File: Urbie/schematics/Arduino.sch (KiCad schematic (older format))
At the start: 1 part

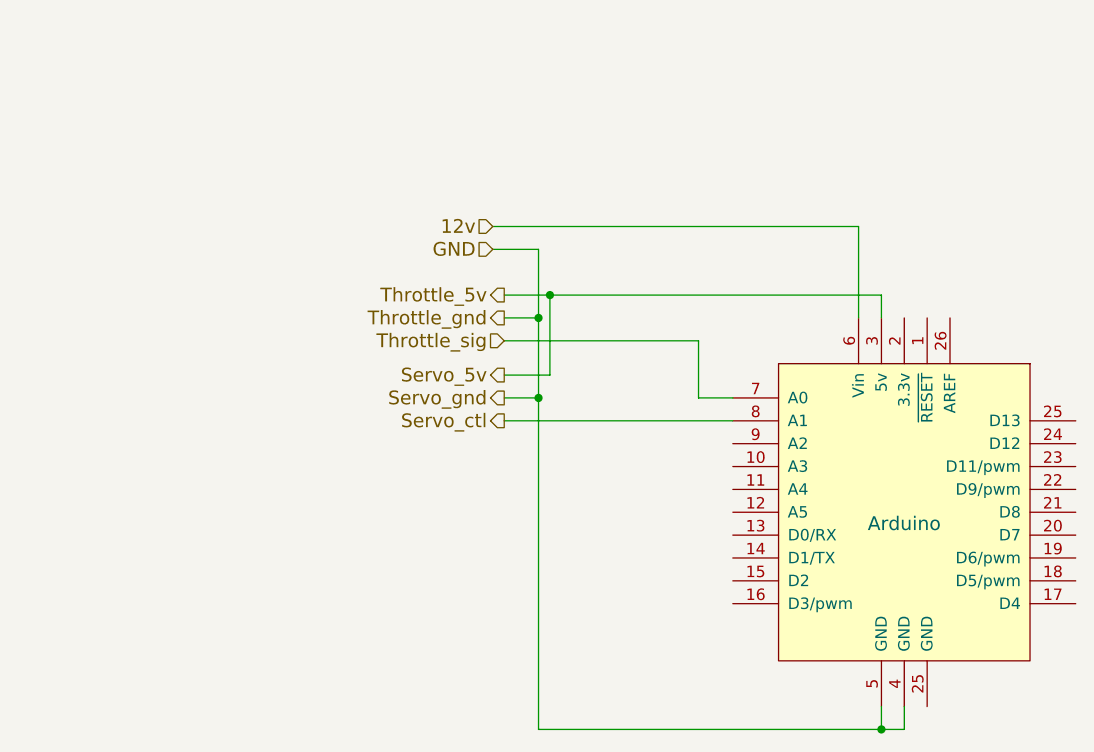
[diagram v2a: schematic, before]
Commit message: added DPDT switch for Hazard lights on Urbie
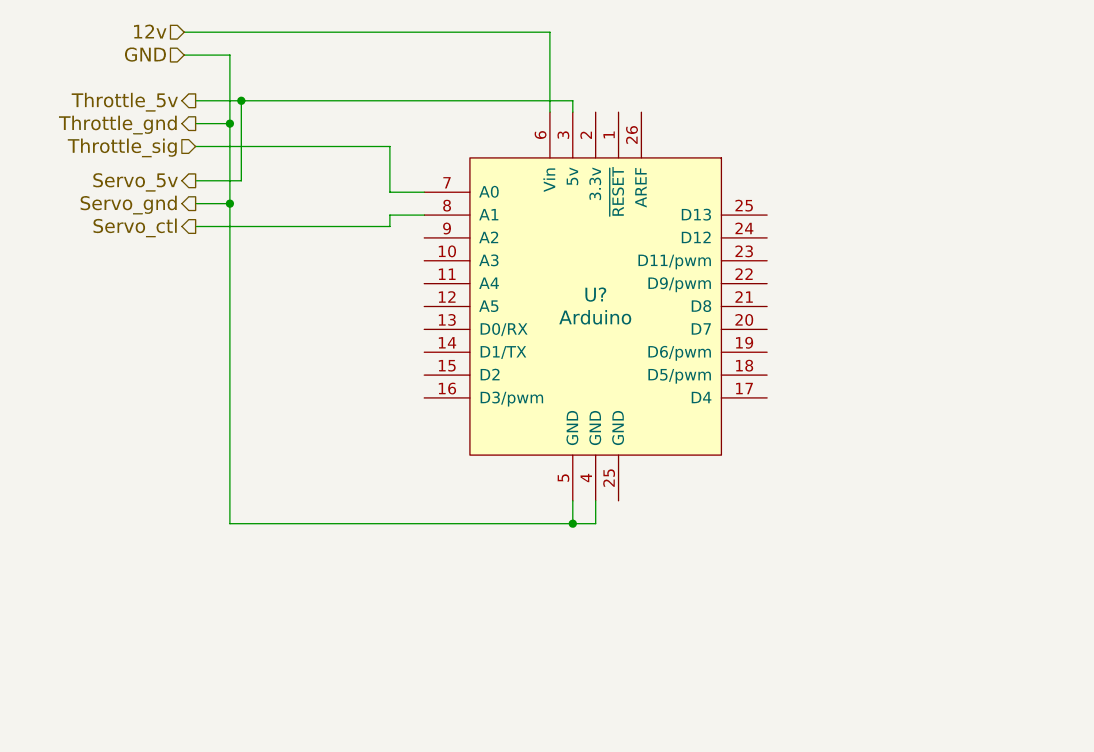
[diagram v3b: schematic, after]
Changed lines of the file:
@@
 LIBS:Supermileage
 LIBS:UrbieSchematics-cache
-LIBS:EFI_Breakout-cache
 EELAYER 25 0
 EELAYER END
 $Descr USLetter 11000 8500
 encoding utf-8
-Sheet 4 6
-Title "Urbie - Gasoline Urban Concept"
-Date "2016-11-19"
+Sheet 5 6
+Title "Sting - Gasoline Prototype"
+Date ""
 Rev ""
 Comp "Cedarville University"
-Comment1 "Tineka Witt"
+Comment1 "Samuel Ellicott"
 Comment2 "Arduino wiring connections"
 Comment3 ""
@@
 L Arduino U?
 U 1 1 57A2439F
-P 5900 4200
-F 0 "U?" H 5900 4250 60  0001 C CNN
-F 1 "Arduino" H 5900 4150 60  0000 C CNN
-F 2 "" H 5900 4500 60  0000 C CNN
-F 3 "" H 5900 4500 60  0000 C CNN
-	1    5900 4200
+P 4550 3300
+F 0 "U?" H 4550 3350 60  0000 C CNN
+F 1 "Arduino" H 4550 3250 60  0000 C CNN
+F 2 "" H 4550 3600 60  0000 C CNN
+F 3 "" H 4550 3600 60  0000 C CNN
+	1    4550 3300
 	1    0    0    -1
 $EndComp
-Text HLabel 4100 2950 0    60   Input ~ 0
+Text HLabel 2750 2100 0    60   Input ~ 0
 12v
-Text HLabel 4100 3050 0    60   Input ~ 0
+Text HLabel 2750 2200 0    60   Input ~ 0
 GND
-Text HLabel 4150 3250 0    60   Output ~ 0
+Text HLabel 2800 2400 0    60   Output ~ 0
 Throttle_5v
-Text HLabel 4150 3350 0    60   Output ~ 0
+Text HLabel 2800 2500 0    60   Output ~ 0
 Throttle_gnd
-Text HLabel 4150 3450 0    60   Input ~ 0
+Text HLabel 2800 2600 0    60   Input ~ 0
 Throttle_sig
-Text HLabel 4150 3600 0    60   Output ~ 0
+Text HLabel 2800 2750 0    60   Output ~ 0
 Servo_5v
-Text HLabel 4150 3700 0    60   Output ~ 0
+Text HLabel 2800 2850 0    60   Output ~ 0
 Servo_gnd
-Text HLabel 4150 3800 0    60   Output ~ 0
+Text HLabel 2800 2950 0    60   Output ~ 0
 Servo_ctl
 Wire Wire Line
-	4100 3050 4300 3050
+	2750 2200 2950 2200
 Wire Wire Line
-	4300 3050 4300 5150
+	2950 2200 2950 4250
 Wire Wire Line
-	5700 2950 5700 3350
+	4350 2100 4350 2450
 Wire Wire Line
-	5700 2950 4100 2950
+	4350 2100 2750 2100
 Wire Wire Line
-	4150 3250 5800 3250
+	2800 2400 4450 2400
 Wire Wire Line
-	4350 3250 4350 3600
+	3000 2400 3000 2750
 Wire Wire Line
-	4350 3600 4150 3600
+	3000 2750 2800 2750
 Wire Wire Line
-	4300 3350 4150 3350
+	2950 2500 2800 2500
 Wire Wire Line
-	4300 3700 4150 3700
-Connection ~ 4300 3350
-Connection ~ 4300 3700
+	2950 2850 2800 2850
+Connection ~ 2950 2500
+Connection ~ 2950 2850
 Wire Wire Line
-	4150 3800 5150 3800
+	2800 2950 3650 2950
 Wire Wire Line
-	5000 3800 5000 3800
+	3650 2900 3800 2900
 Wire Wire Line
-	4150 3450 5000 3450
+	3650 2950 3650 2900
 Wire Wire Line
-	5000 3450 5000 3700
+	2800 2600 3650 2600
 Wire Wire Line
-	5000 3700 5150 3700
+	3650 2600 3650 2800
 Wire Wire Line
-	5800 3250 5800 3350
-Connection ~ 4350 3250
+	3650 2800 3800 2800
 Wire Wire Line
-	4300 5150 5900 5150
+	4450 2400 4450 2450
+Connection ~ 3000 2400
 Wire Wire Line
-	5800 5150 5800 5050
+	2950 4250 4550 4250
 Wire Wire Line
-	5900 5150 5900 5050
-Connection ~ 5800 5150
+	4450 4250 4450 4150
+Wire Wire Line
+	4550 4250 4550 4150
+Connection ~ 4450 4250
 $EndSCHEMATC
